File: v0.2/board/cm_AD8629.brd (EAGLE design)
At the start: 68.9 x 59.7 mm, 106 parts, among them J1 USB_A_SMT_FEMALE

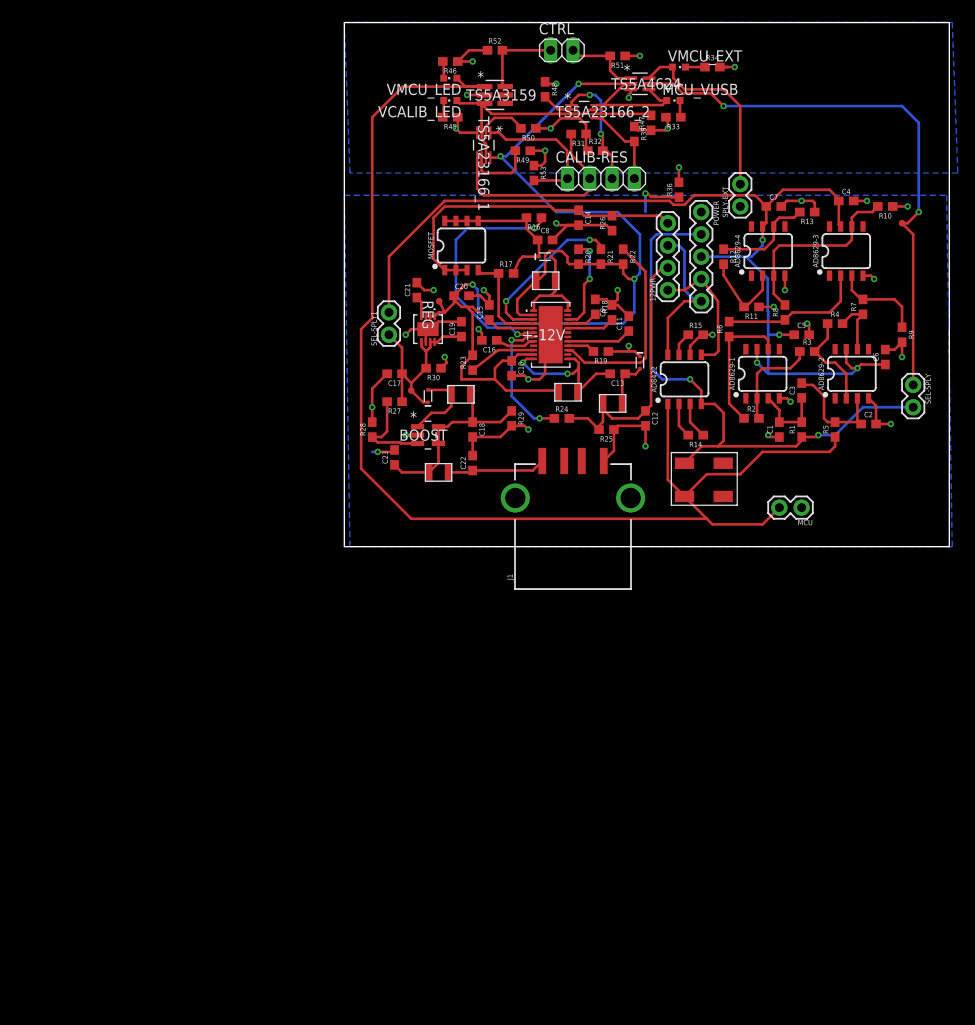
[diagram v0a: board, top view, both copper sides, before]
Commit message: add usb ports to schematics
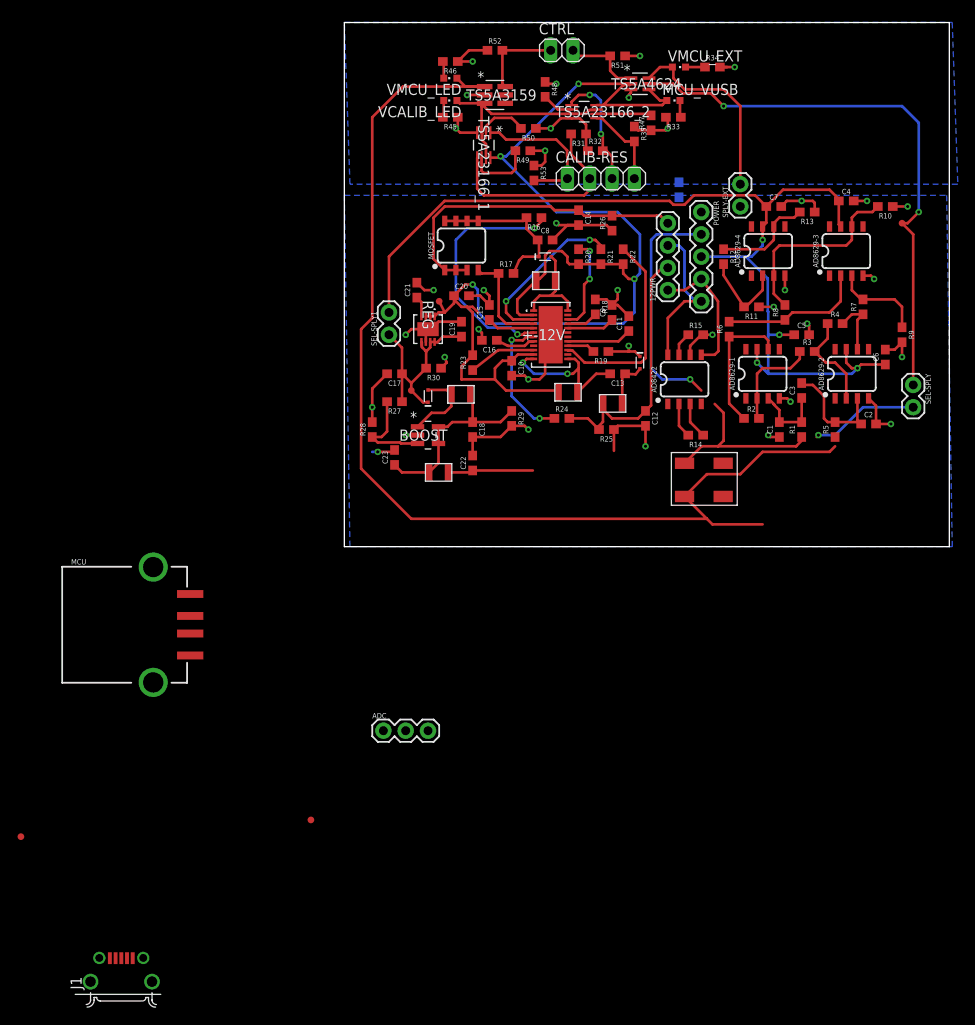
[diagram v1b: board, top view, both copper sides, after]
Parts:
- added ADC: 455-1750-1-ND, SparkFun-Connectors:1X03
- added TP1, TP2: TEST-POINT3, SparkFun-Connectors:PAD.03X.03
- J1: value USB_A_SMT_FEMALE -> 10118194-0001LF; device SparkFun-Connectors:USB-A-S-SILK-FEMALE -> 10118194-0001LF:FRAMATOME_10118194-0001LF
- MCU: value (none) -> USB_A_SMT_FEMALE; device SparkFun-Connectors:1X02 -> SparkFun-Connectors:USB-A-S-SILK-FEMALE
- moved MCU 78.0 mm to (-24.8, -6.99), turned to 0 degrees
- moved J1 73.2 mm to (-25.4, -47.6), turned to 0 degrees
- flipped R36 to the bottom
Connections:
- removed net N$11: AD8422.7, R15.1
- removed net N$15: J1.D+
- removed net N$16: J1.D-
- removed net N$18: AD8629-4.6, R12.1, R13.2
- new net D+: J1.3
- new net D-: J1.2
- new net SHUNT+: AD8422.4, R1.1, U$1.SUPD
- new net SHUNT-: AD8422.1, R5.1, U$1.INFD
- new net VHOUT: AD8422.7, ADC.3, R15.1
- new net VLOUT: AD8629-4.6, ADC.2, R12.1, R13.2
- net 5VIN: no longer J1.VBUS
- net 5VUSB: now also J1.1
- net DGND: now also J1.5
- net GND: now also ADC.1, MCU.GND; no longer J1.GND, MCU.1
- net STG1: now also TP1.P$1
- net VSPLY: no longer AD8422.4, R1.1
- net VSS: now also MCU.VBUS, TP2.P$1; no longer AD8422.1, MCU.2, R5.1
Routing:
- net VSS: track 144.9 -> 129.8 mm
- net VLOUT: track 0.00 -> 11.5 mm
- net N$18: track 11.5 -> 0.00 mm
- net GND: track 115.9 -> 108.2 mm, vias 27 -> 26
- net VSPLY: track 64.8 -> 59.7 mm
- net VHOUT: track 0.00 -> 2.72 mm
- net N$11: track 2.72 -> 0.00 mm
- net DGND: track 39.3 -> 37.6 mm, vias 11 -> 10
- net 5VIN: track 11.2 -> 9.72 mm
